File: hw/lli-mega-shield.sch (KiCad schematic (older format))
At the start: 39 parts, among them K1 36.11.9.003.4000, K2 AC1, K3 PWR source, K4 Encoder 1, K5 AC2, K6 Encoder 2, K7 AC3, K8 LLH UART, P1 Enable, P2 GPS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

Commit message: Made the UP501 GPS module sch and footprint
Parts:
- removed K3: PWR source, symbol CONN_3
- removed P2: GPS, symbol CONN_4
- added J?: DB25, symbol DB25
- added U?: UP500/UP501, symbol UP500/UP501
- U6: value R-78B-1.5 -> R-78B5.0-1.5
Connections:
- wire segments 211 -> 208
- no-connect marks 43 -> 44
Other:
- note added: "Fastrax UP501 default firmware configuration:\n1. Port 0: NMEA 9600 baud\n2. NMEA output: GGA, RMC, GSV, GSA (all 1 sec interval)\n3. DGPS/SBAS: Disabled (Module supports WAAS/EGNOS)\n4. Datum: WGS84"
- note added: "If pull up resistors is needed,\nenable them in the AVR"
- note added: "The footprint\nis in the form\nof a 26 pin\nheader array"
- note added: "Using Arduino\nUSB connection"
- note removed: "If pull up\nresistors\nis needed,\nenable them\nin the AVR"
- note removed: "Jumper to select supply voltage\nfor the GPS connection"

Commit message: Re arranged outgoing connections to large connector. Stills needs thought son supply design.
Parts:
- removed K2: AC1, symbol CONN_3
- removed K4: Encoder 1, symbol CONN_3
- removed K5: AC2, symbol CONN_3
- removed K6: Encoder 2, symbol CONN_3
- removed K7: AC3, symbol CONN_3
- removed K8: LLH UART, symbol CONN_3
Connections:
- net labels added: DCDIR1, DCDIR2, DCDIR3, DCPWM1, DCPWM2, DCPWM3, RCPWM1, RCPWM2, RCPWM3, RL_BATT, SCL, SDA
- net labels removed: LLH_RX, LLH_TX
- wire segments 208 -> 194
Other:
- note added: "3.3 V from Arduino\n 5.0 V from Arduino\n 5.0 V seperatly directly from battery packs\n14.8 V battery supply"
- note added: "Bow thruster"
- note added: "I2C"
- note added: "I2C not planned for any use"
- note added: "Quadrature\nencoder input"
- note added: "RCPWMx is common RC\npulse standard while\nthe DCPWMx is common\nPWM with dutycycle\n0-100%"
- note added: "RL_BATT and +5VP has to be\nactivated by the microcontroller"
- note added: "Thrusters"
- note removed: "3.3 V from Arduino\n 5.0 V from Arduino\n 5.0 V seperatly directly from battery packs\n14.4 V battery supply"
- note removed: "LLH UART"
- note removed: "PWM controlled actuators"
- note removed: "Quadrature encoder input"
- note removed: "This should probably be\nseperated from the arduino\n5V regulator"
- moved on the sheet: C4, D1, D2, D3, D4, D5, J?, K1, P1, P3, P4, Q1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

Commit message: Some updates to hw
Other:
- note added: "I2C not planned for any use,\nmaybe for OpenServo devices?"
- note removed: "I2C not planned for any use"
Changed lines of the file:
@@
-EESchema Schematic File Version 2  date søn 23 sep 2012 11:40:33 CEST
+EESchema Schematic File Version 2  date søn 23 sep 2012 12:03:57 CEST
 LIBS:power
 LIBS:device
@@
 RL_BATT
 Text Notes 2400 2350 0    60   ~ 0
-I2C not planned for any use
+I2C not planned for any use,\nmaybe for OpenServo devices?
 Text Notes 4850 2350 2    60   ~ 0
 I2C

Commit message: Updated schematics to conform with a DB25 connector
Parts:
- removed P3: AUX A, symbol CONN_5X2
- removed P4: AUX B, symbol CONN_5X2
- removed U3, U4: LM35, symbol LM35
- gave numbers to parts that had none: 2
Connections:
- net AC1 is gone; now on net DCDIR1: SHIELD1.AD0
- net AC2 is gone; now on net DCDIR2: SHIELD1.AD1
- net AC3 is gone; now on net DCDIR3: SHIELD1.AD2
- net +5VP: now also J1.3
- net +BATT: now also J1.14 (P14), J1.15 (P15)
- net DCPWM1: now also SHIELD1.2
- net DCPWM2: now also SHIELD1.3
- net DCPWM3: now also SHIELD1.5
- net GND: now also J1.2; no longer J1.14 (P14)
- net IRQ: now also SHIELD1.AD7
- net RCPWM1: now also SHIELD1.11
- net RCPWM2: now also SHIELD1.12
- net RCPWM3: now also SHIELD1.13
- net RF_EN: now also SHIELD1.AD12
- net RL_BATT: now also J1.16 (P16)
- net SCL: now also J1.5; no longer J1.6
- net SDA: now also J1.18 (P18); no longer J1.19 (P19)
- net T2: now also J1.17 (P17)
- net T3: now also J1.4
- net ~RST: now also SHIELD1.AD6
- net RCPWM4: now reaches SHIELD1.7
- net RCPWM4: now also J1.21 (P21)
- net RCPWM5: now reaches SHIELD1.8
- net RCPWM5: now also J1.8
- net AUX_A1: no longer names the net of SHIELD1.22 (PA0)
- net AUX_A2: no longer names the net of SHIELD1.23 (PA1)
- net AUX_A3: no longer names the net of SHIELD1.24 (PA2)
- net AUX_A4: no longer names the net of SHIELD1.25 (PA3)
- net AUX_A5: no longer names the net of SHIELD1.26 (PA4)
- net AUX_A6: no longer names the net of SHIELD1.27 (PA5)
- net AUX_B1: no longer names the net of SHIELD1.28 (PA6)
- net AUX_B2: no longer names the net of SHIELD1.29 (PA7)
- net AUX_B3: no longer names the net of SHIELD1.30 (PC7)
- net AUX_B4: no longer names the net of SHIELD1.31 (PC6)
- net AUX_B5: no longer names the net of SHIELD1.32 (PC5)
- net AUX_B6: no longer names the net of SHIELD1.33 (PC4)
- net DIO2: no longer names the net of U5.9 (DIO2)
- net DIO3: no longer names the net of U5.1 (DIO3)
- net DIO4: no longer names the net of U5.2 (DIO4/CLKIN)
- net ENC1_A renamed IO1
- net IO1: now also J1.20 (P20); no longer J1.21 (P21)
- net ENC1_B renamed IO2
- net IO2: now also J1.7; no longer J1.8
- net ENC2_A renamed IO3
- net IO3: now also J1.19 (P19); no longer J1.20 (P20)
- net ENC2_B renamed IO4
- net IO4: now also J1.6; no longer J1.7
- no-connect marks 44 -> 46
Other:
- note added: "+5VP switch\nregulator needs\nno flag to pass\nDRC"
- note added: "Aux. IO\n(PCINTx)"
- note added: "Aux. servo"
- note added: "Auxiliary Input/Output pins, can\nalso be used with the ADC."
- note added: "Auxiliary\nInput/Output"
- note added: "DCPWM\n(OC3 timer)"
- note added: "DCPWMx PWM pulse for 0-100% duty cycle for custom H-bridge like driver\nDCDIRx direction control for the H-bridge like dirver\nRCPWM RC standard 50 Hz 1-2ms signal"
- note added: "External sensors to be mounted\ni.e. on the motors."
- note added: "External\ntemperature"
- note added: "IMU IRQ"
- note added: "IMU Reset"
- note added: "IMU SPI"
- note added: "Interface connector"
- note added: "Note"
- note added: "Pin mapping"
- note added: "RCPWM\n(OC1 timer)"
- note added: "RCPWM\n(OC4 timer)"
- note added: "RF enable"
- note added: "Rudder servo"
- note added: "Use"
- note removed: "Encoder"
- note removed: "Encoder pins is connected to\nhardware pin change interrups"
- note removed: "Quadrature\nencoder input"
- note removed: "The footprint\nis in the form\nof a 26 pin\nheader array"
- moved on the sheet: C2, C3, J1, R3, R4

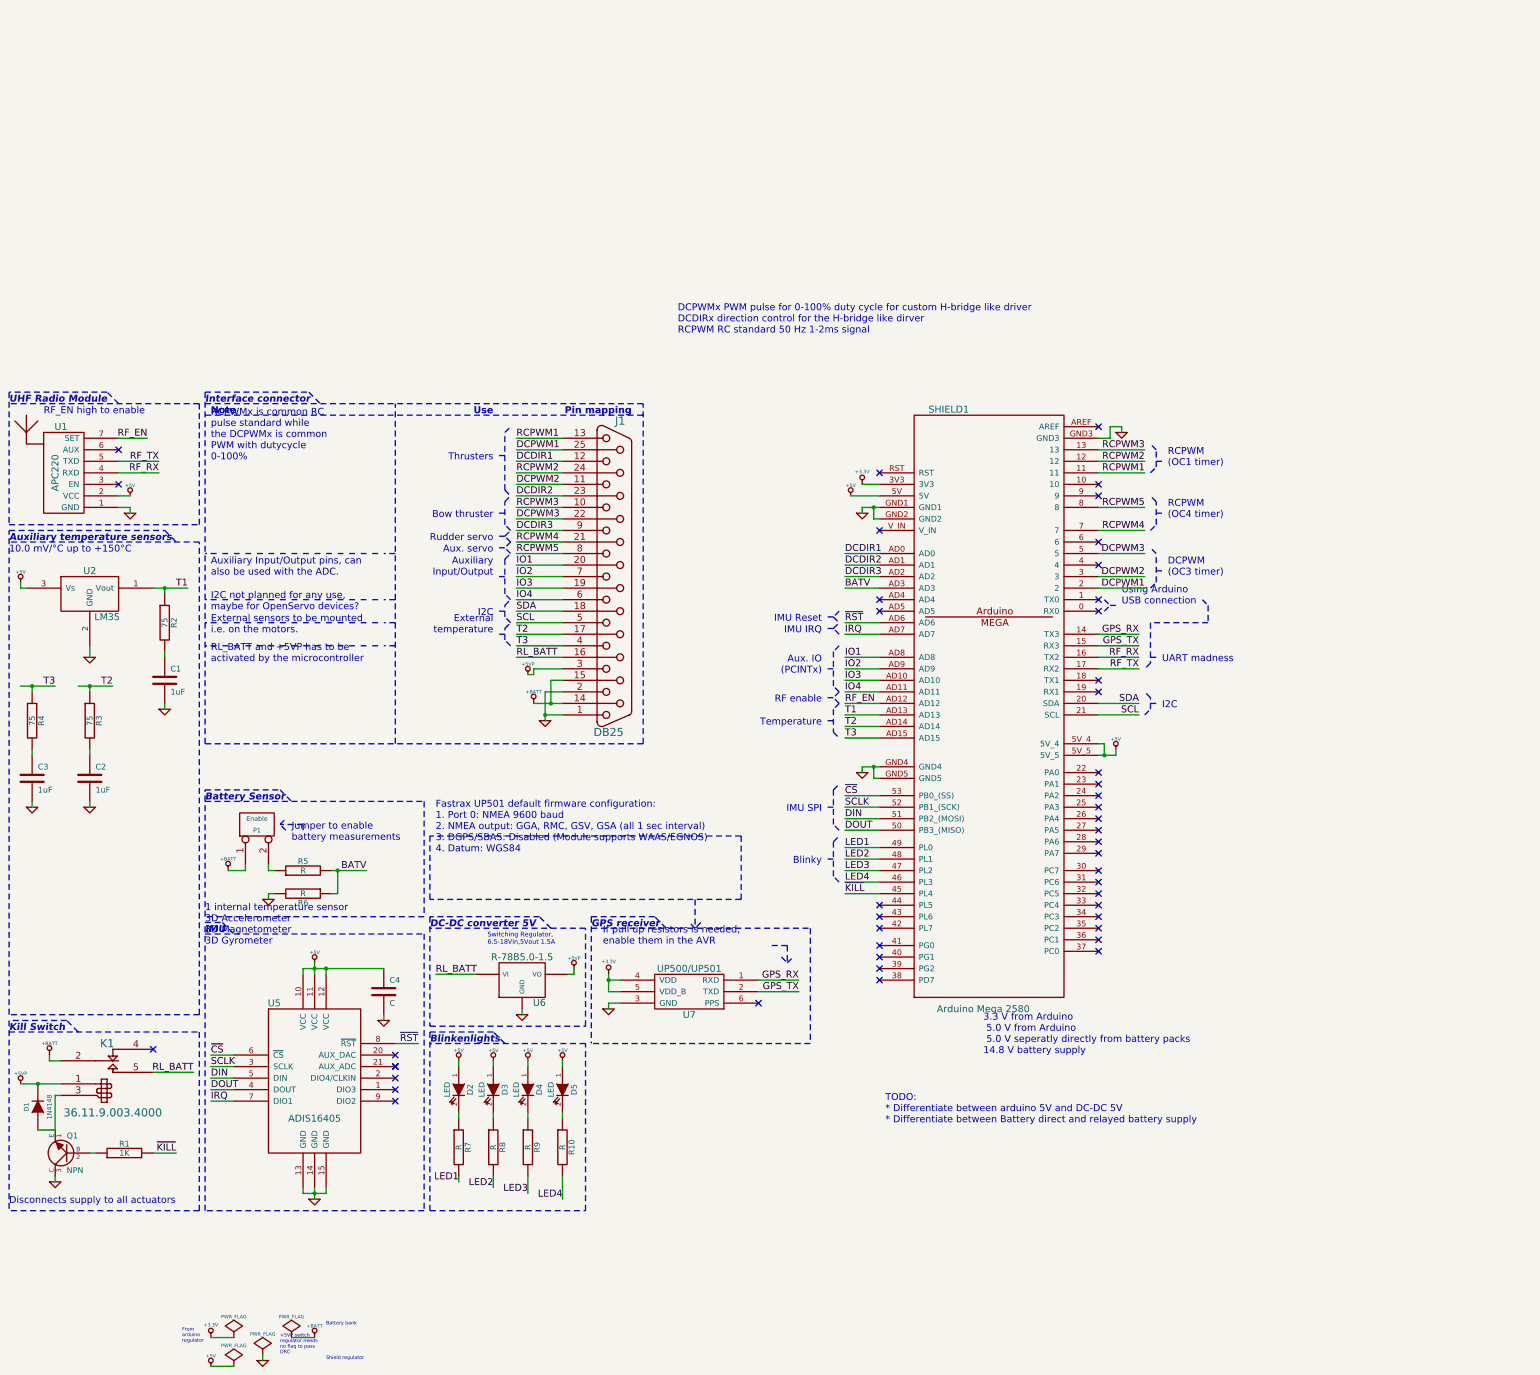
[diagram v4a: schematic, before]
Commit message: Now the layout has to be optimized for the header conn
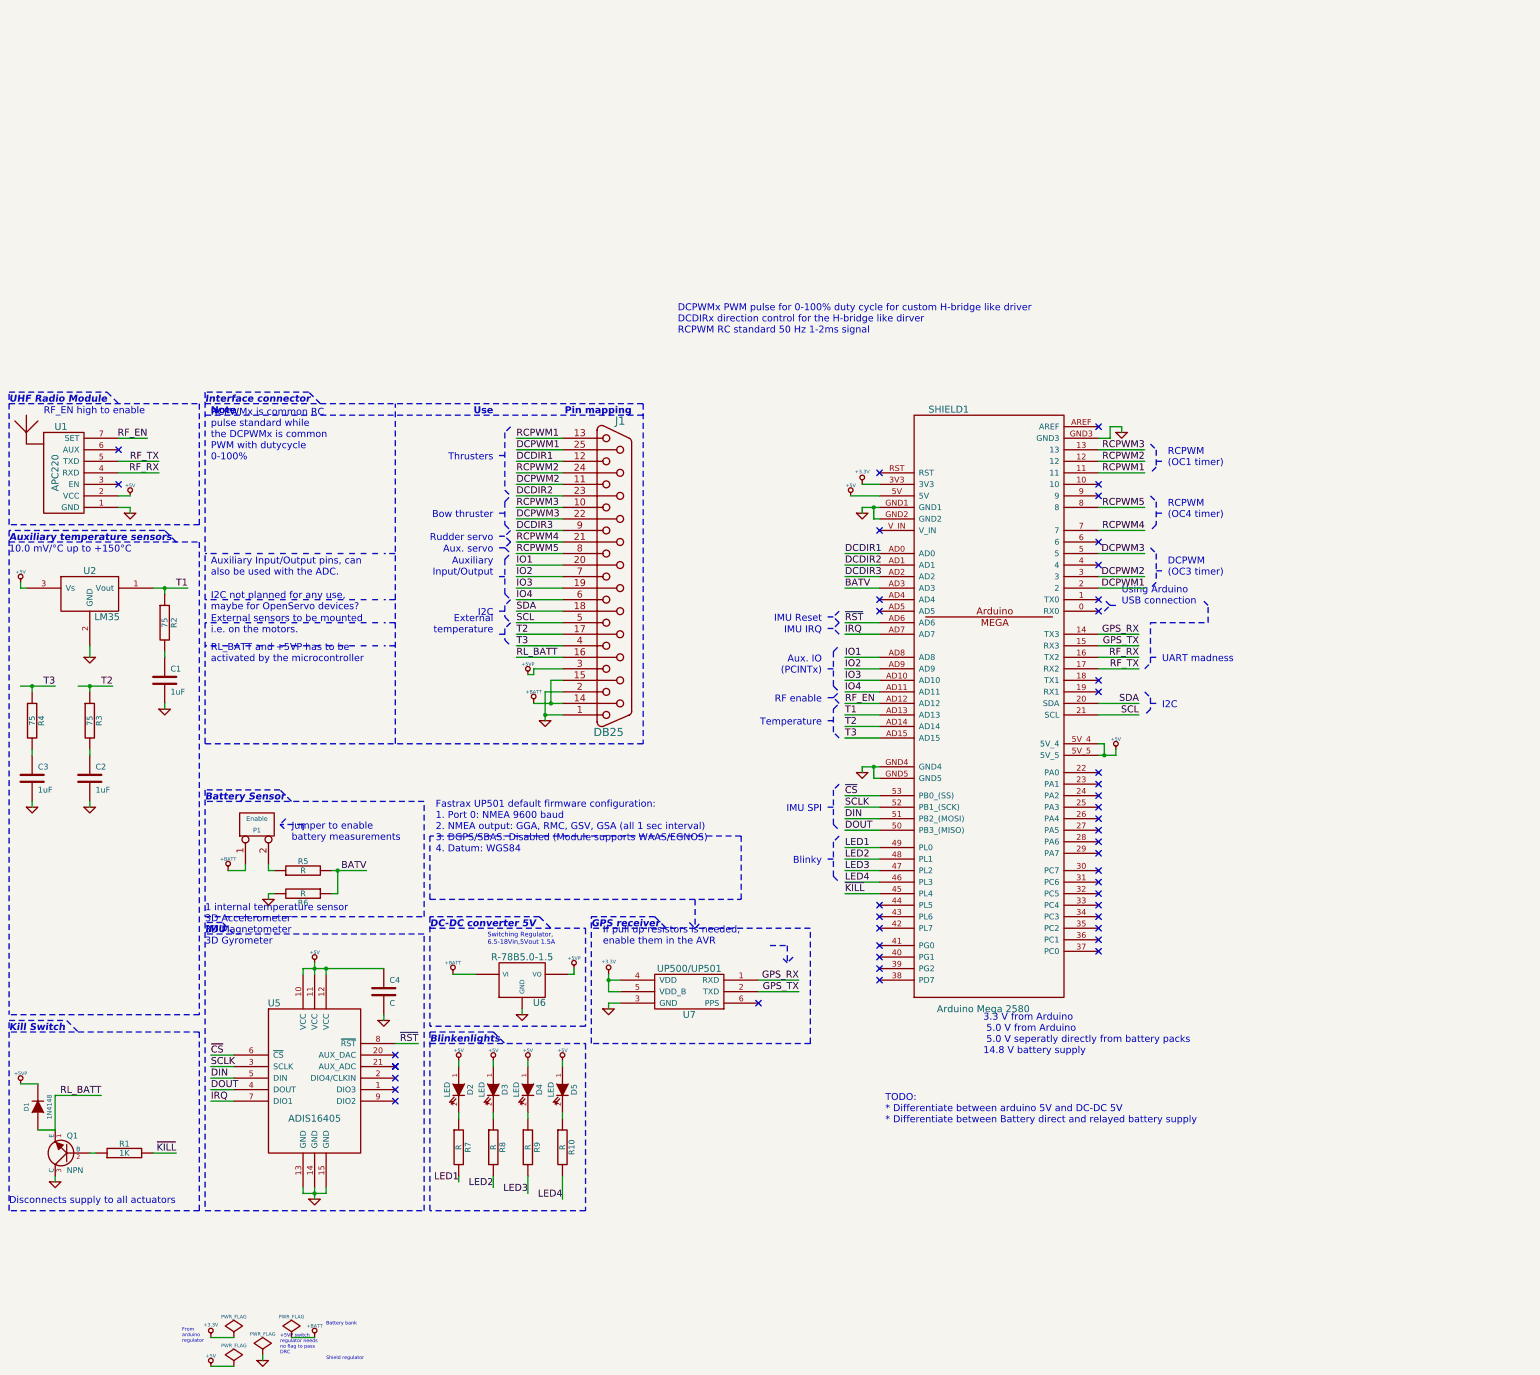
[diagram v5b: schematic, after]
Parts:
- removed K1: 36.11.9.003.4000, symbol RELAY_1RT
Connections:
- net +BATT: now also U6.VI
- net RL_BATT: now also D1.1 (A), Q1.1 (E); no longer U6.VI
- no-connect marks 46 -> 45

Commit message: Updated a note
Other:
- note added: "Auxiliary Input/Output pins, can\nalso be used with the ADC. Comms\nwith advanced survailence of power\nsplitter."
- note removed: "Auxiliary Input/Output pins, can\nalso be used with the ADC."
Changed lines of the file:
@@
-EESchema Schematic File Version 2  date søn 30 sep 2012 19:45:06 CEST
+EESchema Schematic File Version 2  date søn 30 sep 2012 20:16:28 CEST
 LIBS:power
 LIBS:device
@@
 Text Notes 8150 6950 0    60   ~ 0
 TODO:\n* Differentiate between arduino 5V and DC-DC 5V\n* Differentiate between Battery direct and relayed battery supply
-Text Notes 2300 2200 0    60   ~ 0
-Auxiliary Input/Output pins, can\nalso be used with the ADC.
+Text Notes 2300 2100 0    60   ~ 0
+Auxiliary Input/Output pins, can\nalso be used with the ADC. Comms\nwith advanced survailence of power\nsplitter.
 Text Label 4950 2100 0    60   ~ 0
 IO1
